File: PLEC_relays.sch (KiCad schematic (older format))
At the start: 19 parts, among them K2 PB1167, K3 PB1167, K4 PB1167, U3 TLP222A-2, U4 TLP222A, U5 TLP222A-2

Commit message: Almost done with layout; need to rearrange uC pins
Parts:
- renumbered C14 to C10, C15 to C11, C16 to C12, C17 to C13, C18 to C14, C19 to C15, C12 to C8, C13 to C9, R29 to R27, R30 to R28, R31 to R29, R32 to R30, R33 to R31
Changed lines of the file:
@@
 VSS
 $Comp
-L R R29
+L R R27
 U 1 1 5A74E273
 P 5500 1300
-F 0 "R29" V 5580 1300 50  0000 C CNN
+F 0 "R27" V 5580 1300 50  0000 C CNN
 F 1 "100K" V 5500 1300 50  0000 C CNN
 F 2 "Resistors_THT:R_Axial_DIN0204_L3.6mm_D1.6mm_P5.08mm_Horizontal" V 5430 1300 50  0001 C CNN
@@
 $EndComp
 $Comp
-L R R30
+L R R28
 U 1 1 5A74E434
 P 5500 2550
-F 0 "R30" V 5580 2550 50  0000 C CNN
+F 0 "R28" V 5580 2550 50  0000 C CNN
 F 1 "100K" V 5500 2550 50  0000 C CNN
 F 2 "Resistors_THT:R_Axial_DIN0204_L3.6mm_D1.6mm_P5.08mm_Horizontal" V 5430 2550 50  0001 C CNN
@@
 Connection ~ 5500 2750
 $Comp
-L R R33
+L R R31
 U 1 1 5A74E6F3
 P 5500 6950
-F 0 "R33" V 5580 6950 50  0000 C CNN
+F 0 "R31" V 5580 6950 50  0000 C CNN
 F 1 "100K" V 5500 6950 50  0000 C CNN
 F 2 "Resistors_THT:R_Axial_DIN0204_L3.6mm_D1.6mm_P5.08mm_Horizontal" V 5430 6950 50  0001 C CNN
@@
 	5500 7100 5500 7150
 $Comp
-L C C15
+L C C11
 U 1 1 5A74E708
 P 5750 1300
-F 0 "C15" H 5775 1400 50  0000 L CNN
+F 0 "C11" H 5775 1400 50  0000 L CNN
 F 1 "4700p" H 5775 1200 50  0000 L CNN
 F 2 "PLEC:THTt_100Px150Lx100Wx183H_4700p" H 5788 1150 50  0001 C CNN
@@
 Connection ~ 5750 1500
 $Comp
-L C C19
+L C C15
 U 1 1 5A74E84A
 P 5750 6950
-F 0 "C19" H 5775 7050 50  0000 L CNN
+F 0 "C15" H 5775 7050 50  0000 L CNN
 F 1 "4700p" H 5775 6850 50  0000 L CNN
 F 2 "PLEC:THTt_100Px150Lx100Wx183H_4700p" H 5788 6800 50  0001 C CNN
@@
 	5750 7100 5750 7150
 $Comp
-L C C16
+L C C12
 U 1 1 5A74EB29
 P 5750 2550
-F 0 "C16" H 5775 2650 50  0000 L CNN
+F 0 "C12" H 5775 2650 50  0000 L CNN
 F 1 "4700p" H 5775 2450 50  0000 L CNN
 F 2 "PLEC:THTt_100Px150Lx100Wx183H_4700p" H 5788 2400 50  0001 C CNN
@@
 $EndComp
 $Comp
-L R R31
+L R R29
 U 1 1 5A74EC6B
 P 5500 4550
-F 0 "R31" V 5580 4550 50  0000 C CNN
+F 0 "R29" V 5580 4550 50  0000 C CNN
 F 1 "100K" V 5500 4550 50  0000 C CNN
 F 2 "Resistors_THT:R_Axial_DIN0204_L3.6mm_D1.6mm_P5.08mm_Horizontal" V 5430 4550 50  0001 C CNN
@@
 	5500 4700 5500 4750
 $Comp
-L C C17
+L C C13
 U 1 1 5A74EC73
 P 5750 4550
-F 0 "C17" H 5775 4650 50  0000 L CNN
+F 0 "C13" H 5775 4650 50  0000 L CNN
 F 1 "4700p" H 5775 4450 50  0000 L CNN
 F 2 "PLEC:THTt_100Px150Lx100Wx183H_4700p" H 5788 4400 50  0001 C CNN
@@
 Connection ~ 5500 4750
 $Comp
-L R R32
+L R R30
 U 1 1 5A74ED9D
 P 5500 5700
-F 0 "R32" V 5580 5700 50  0000 C CNN
+F 0 "R30" V 5580 5700 50  0000 C CNN
 F 1 "100K" V 5500 5700 50  0000 C CNN
 F 2 "Resistors_THT:R_Axial_DIN0204_L3.6mm_D1.6mm_P5.08mm_Horizontal" V 5430 5700 50  0001 C CNN
@@
 	5500 5850 5500 5900
 $Comp
-L C C18
+L C C14
 U 1 1 5A74EDA5
 P 5750 5700
-F 0 "C18" H 5775 5800 50  0000 L CNN
+F 0 "C14" H 5775 5800 50  0000 L CNN
 F 1 "4700p" H 5775 5600 50  0000 L CNN
 F 2 "PLEC:THTt_100Px150Lx100Wx183H_4700p" H 5788 5550 50  0001 C CNN
@@
 VDD
 $Comp
-L C C12
+L C C8
 U 1 1 5A770528
 P 1800 2450
-F 0 "C12" H 1825 2550 50  0000 L CNN
+F 0 "C8" H 1825 2550 50  0000 L CNN
 F 1 "470u" H 1825 2350 50  0000 L CNN
 F 2 "PLEC:THTm_5Px8Dx22H__470u" H 1838 2300 50  0001 C CNN
@@
 VSS
 $Comp
-L C C14
+L C C10
 U 1 1 5A7707AC
 P 2500 2450
-F 0 "C14" H 2525 2550 50  0000 L CNN
+F 0 "C10" H 2525 2550 50  0000 L CNN
 F 1 "4.7u" H 2525 2350 50  0000 L CNN
 F 2 "PLEC:THTm_1.5Px4Dx7H_4.7u" H 2538 2300 50  0001 C CNN
@@
 Connection ~ 2500 2700
 $Comp
-L C C13
+L C C9
 U 1 1 5A75F71C
 P 2150 2450
-F 0 "C13" H 2175 2550 50  0000 L CNN
+F 0 "C9" H 2175 2550 50  0000 L CNN
 F 1 "47u" H 2175 2350 50  0000 L CNN
 F 2 "PLEC:THTm_2Px4Dx12H_47u" H 2188 2300 50  0001 C CNN

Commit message: Finished PCB with no errors
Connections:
- net R3D_SUPPLY: now reaches K2.4, U4.3
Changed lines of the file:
@@
 Wire Wire Line
 	1600 2200 2500 2200
+Text Label 3300 3550 0    60   ~ 0
+R3D_SUPPLY
 $EndSCHEMATC

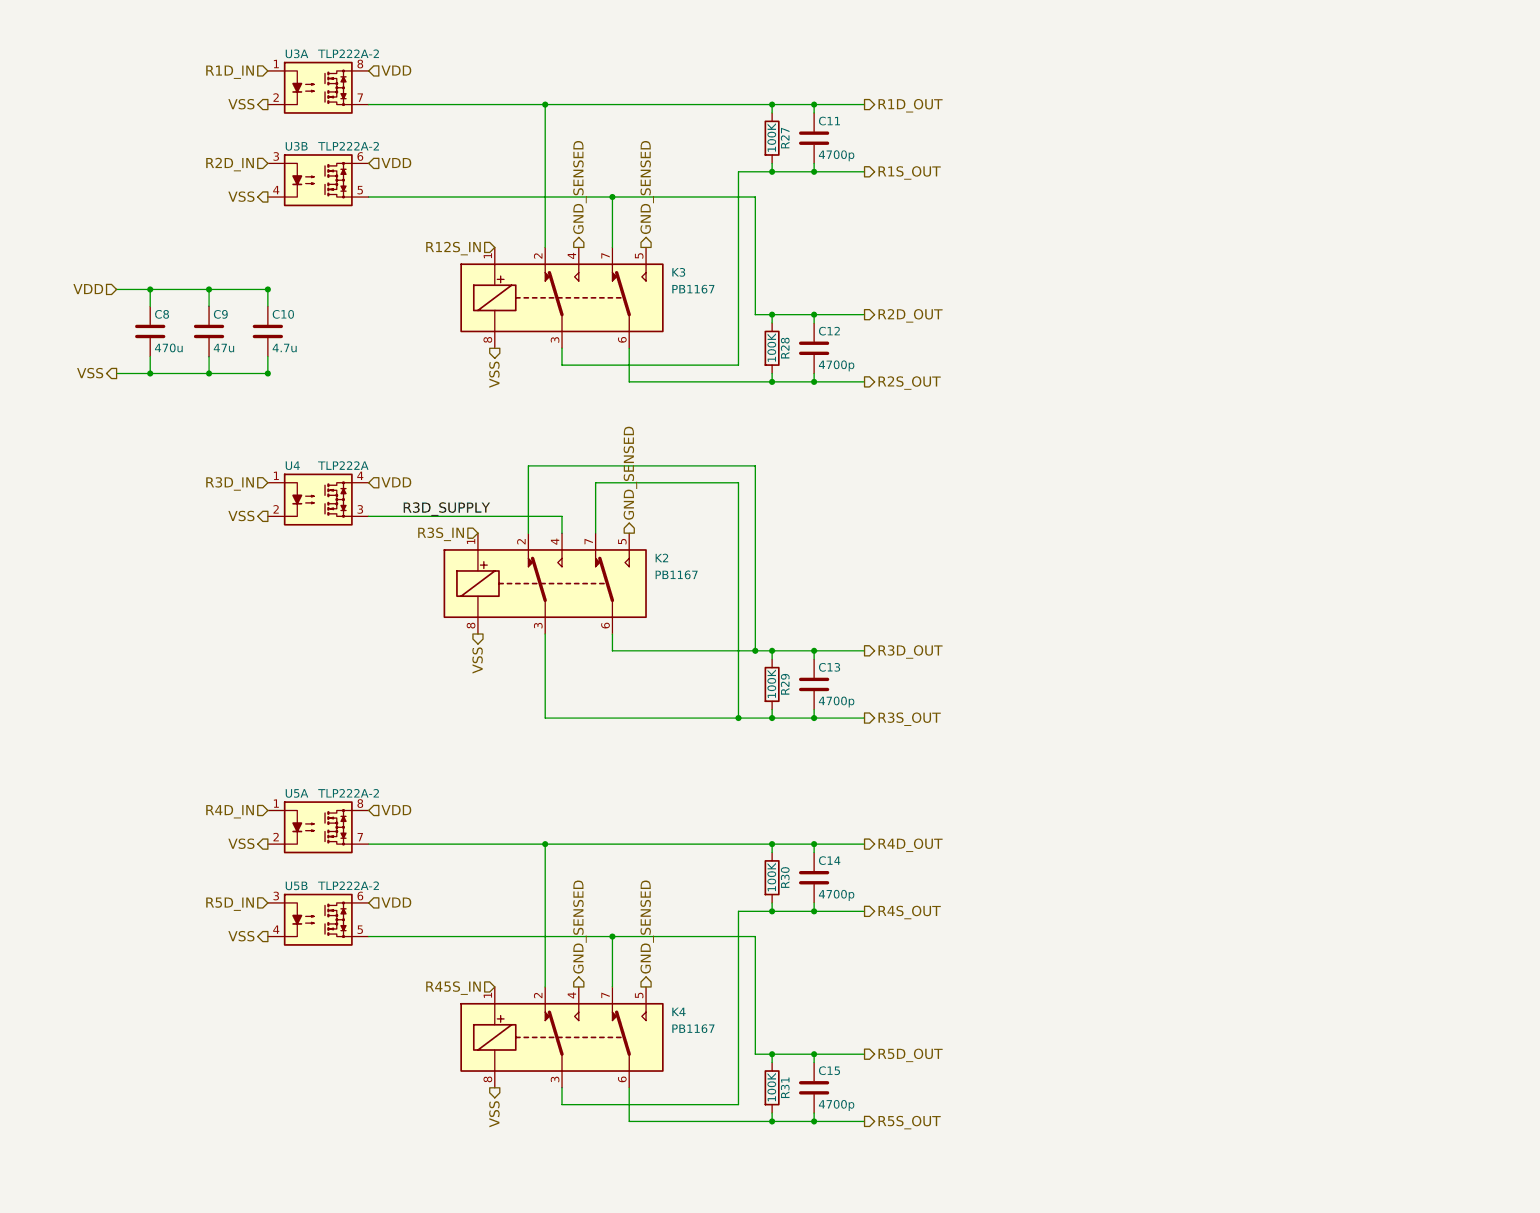
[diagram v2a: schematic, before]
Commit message: Replaced solid state relays with NPN Darlingtons
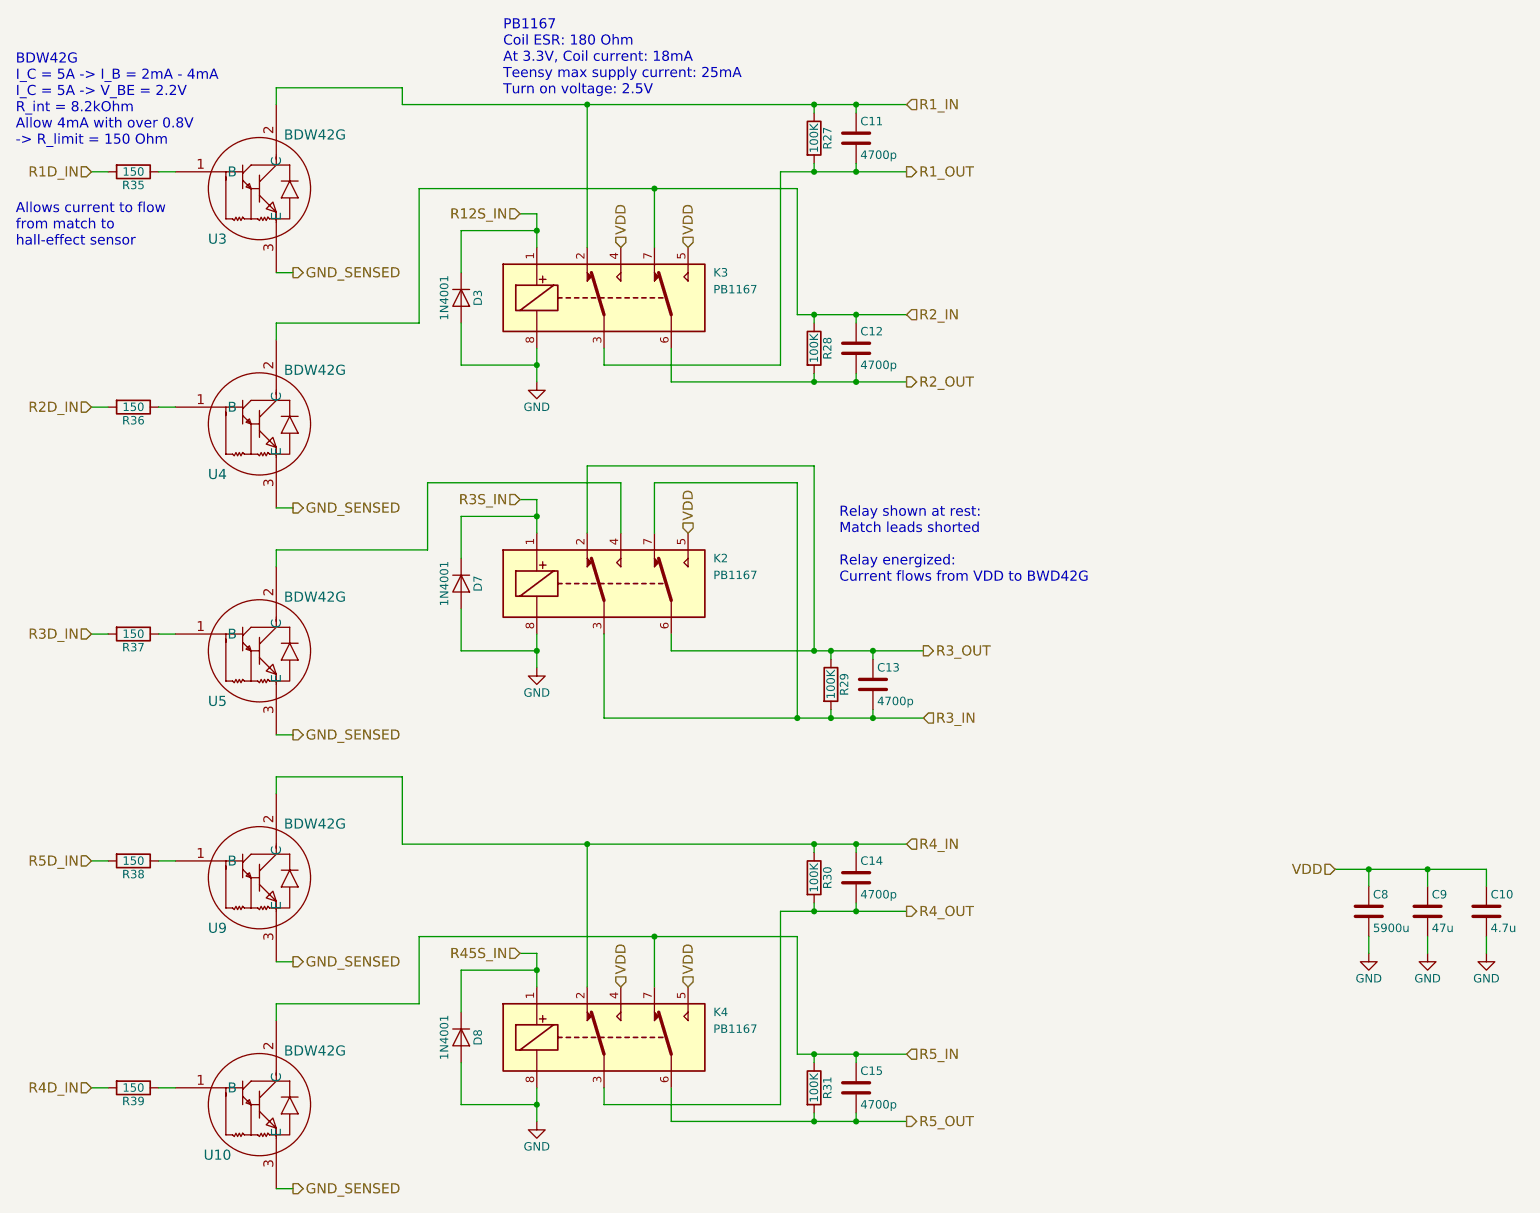
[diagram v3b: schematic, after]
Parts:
- removed U3, U5: TLP222A-2, Housings_DIP:DIP-8_W7.62mm, symbol TLP222A-2
- removed U4: TLP222A, Housings_DIP:DIP-4_W7.62mm, symbol TLP222A
- added D3, D7, D8: 1N4001, Diodes_THT:D_DO-41_SOD81_P2.54mm_Vertical_KathodeUp, symbol D
- added R35, R36, R37, R38, R39: 150, Resistors_THT:R_Axial_DIN0204_L3.6mm_D1.6mm_P5.08mm_Horizontal, symbol R
- added U10, U3, U4, U5, U9: BDW42G, PLEC:BDW42G, symbol BDW42G
- C8: value 470u -> 5900u; footprint PLEC:THTm_5Px8Dx22H__470u -> PLEC:ELBK250
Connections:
- net GND_SENSED: now also U10.3 (E), U3.3 (E), U4.3 (E), U5.3 (E), U9.3 (E); no longer K2.5, K3.4, K3.5, K4.4, K4.5
- net R12S_IN: now also D3.1 (K)
- net R1D_IN: now also R35.2
- net R2D_IN: now also R36.2
- net R3D_IN: now also R37.2
- net R3S_IN: now also D7.1 (K)
- net R45S_IN: now also D8.1 (K)
- net R4D_IN: now also R39.2
- net R5D_IN: now also R38.2
- net VDD: now also K2.5, K3.4, K3.5, K4.4, K4.5
- net R1D_OUT renamed R1_IN
- net R1_IN: now also U3.2 (C)
- net R1S_OUT renamed R1_OUT
- net R2D_OUT renamed R2_IN
- net R2_IN: now also U4.2 (C)
- net R2S_OUT renamed R2_OUT
- net R3D_OUT renamed R3_OUT
- net R3D_SUPPLY: no longer names the net of K2.4
- net R3D_SUPPLY: now also U5.2 (C)
- net R3S_OUT renamed R3_IN
- net R4D_OUT renamed R4_IN
- net R4_IN: now also U9.2 (C)
- net R4S_OUT renamed R4_OUT
- net R5D_OUT renamed R5_IN
- net R5_IN: now also U10.2 (C)
- net R5S_OUT renamed R5_OUT
- net VSS renamed GND
- net GND: now also D3.2 (A), D7.2 (A), D8.2 (A)
- new net: R36.1, U4.1 (B)
- new net: R37.1, U5.1 (B)
- new net: R39.1, U10.1 (B)
- new net: R38.1, U9.1 (B)
- new net: R35.1, U3.1 (B)
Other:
- note added: "Allows current to flow\nfrom match to\nhall-effect sensor"
- note added: "BDW42G\nI_C = 5A -> I_B = 2mA - 4mA\nI_C = 5A -> V_BE = 2.2V\nR_int = 8.2kOhm\nAllow 4mA with over 0.8V\n-> R_limit = 150 Ohm"
- note added: "PB1167\nCoil ESR: 180 Ohm\nAt 3.3V, Coil current: 18mA\nTeensy max supply current: 25mA\nTurn on voltage: 2.5V"
- note added: "Relay shown at rest:\nMatch leads shorted\n\nRelay energized:\nCurrent flows from VDD to BWD42G"
- moved on the sheet: C10, C11, C12, C13, C14, C15, C8, C9, K2, K3, K4, R27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
